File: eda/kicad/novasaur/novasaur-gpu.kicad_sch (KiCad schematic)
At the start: 26 parts, among them U1 74F86, U28 74F163, U29 74F163, U3 74F11, U30 74F541, U31 74F574, U32 74F574, U33 74F541, U34 74F574, U35 74F299, U36 74F574, U37 74F157

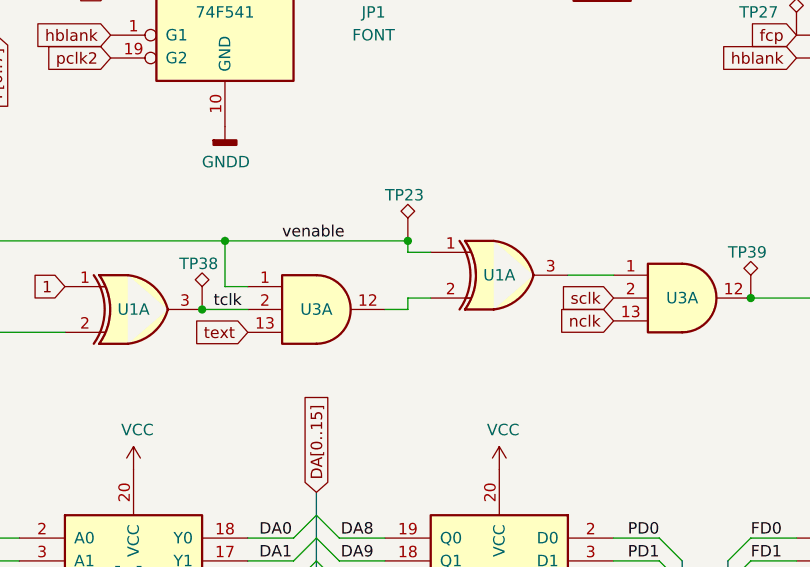
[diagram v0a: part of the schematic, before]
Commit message: Schematic updates
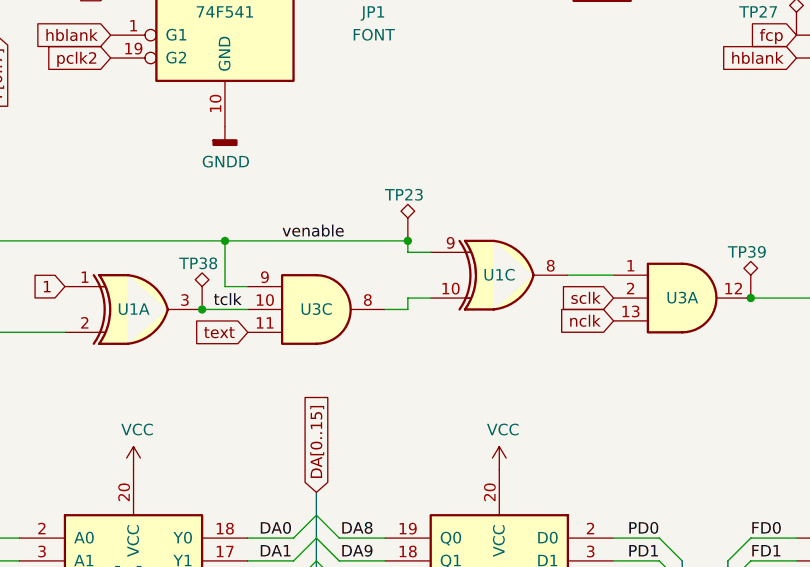
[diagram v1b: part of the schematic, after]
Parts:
- TP26: value ~VOE -> ~{VOE}
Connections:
- net tclk: now also U3.10; no longer U3.2
- net text: now also U3.11; no longer U3.13
- net venable: now also U1.9, U3.9; no longer U1.1, U3.1
- net at U3.1: now also U1.8; no longer U1.3
- new net: U1.10, U3.8
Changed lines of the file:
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@@
   (title_block
     (title "Graphics Processing Unit")
-    (date "2022-03-14")
+    (date "2022-08-07")
     (rev "1.10")
     (comment 1 "(c) Solid State Machines 2022")
@@
       (effects (font (size 1.27 1.27)) (justify left))
     )
-    (property "Value" "~VOE" (id 1) (at 156.21 147.32 0)
+    (property "Value" "~{VOE}" (id 1) (at 156.21 147.32 0)
       (effects (font (size 1.27 1.27)) (justify left) hide)
     )
@@
     (pin "1")
   )
-  (symbol (lib_id "74xx:74LS86") (at 137.16 88.9 0) (unit 1)
+  (symbol (lib_id "74xx:74LS86") (at 137.16 88.9 0) (unit 3)
     (in_bom yes) (on_board yes)
     (property "Reference" "U1" (id 0) (at 137.16 88.9 0))
@@
       (effects (font (size 1.27 1.27)) hide)
     )
-    (pin "1")
-    (pin "2")
-    (pin "3")
+    (pin "10")
+    (pin "8")
+    (pin "9")
   )
   (symbol (lib_id "74xx:74LS11") (at 157.48 91.44 0) (unit 1)
@@
     (pin "9")
   )
-  (symbol (lib_id "74xx:74LS11") (at 116.84 92.71 0) (unit 1)
+  (symbol (lib_id "74xx:74LS11") (at 116.84 92.71 0) (unit 3)
     (in_bom yes) (on_board yes)
     (property "Reference" "U3" (id 0) (at 116.84 92.71 0))
@@
       (effects (font (size 1.27 1.27)) hide)
     )
-    (pin "1")
-    (pin "12")
-    (pin "13")
-    (pin "2")
+    (pin "10")
+    (pin "11")
+    (pin "8")
+    (pin "9")
   )
   (symbol (lib_id "Connector:TestPoint_Alt") (at 127 85.09 0) (unit 1)
